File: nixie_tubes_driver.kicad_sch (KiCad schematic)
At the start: 17 parts, among them IC1 TPS61041DBVR, U1 CD40109BPW, U5 CD40109BPW, U6 HV5122PG-G, U7 HV5122PG-G

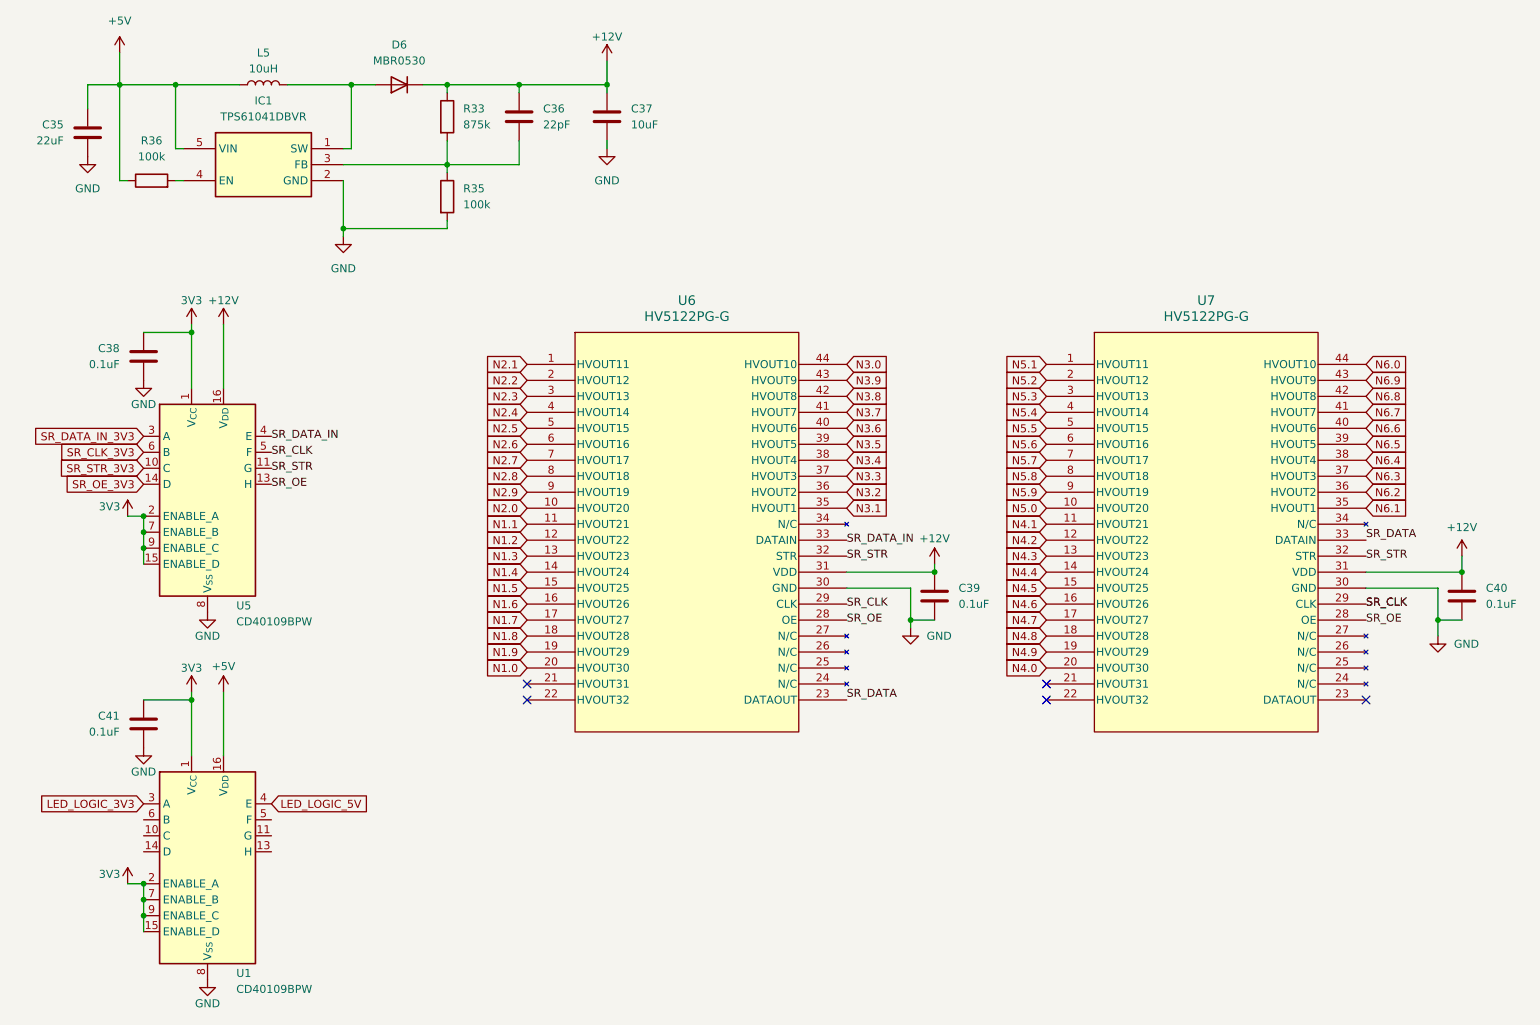
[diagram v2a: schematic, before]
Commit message: Begin positioning and grouping components
Add bypass caps to level shifters Vdd
Rearrange pins on shift register
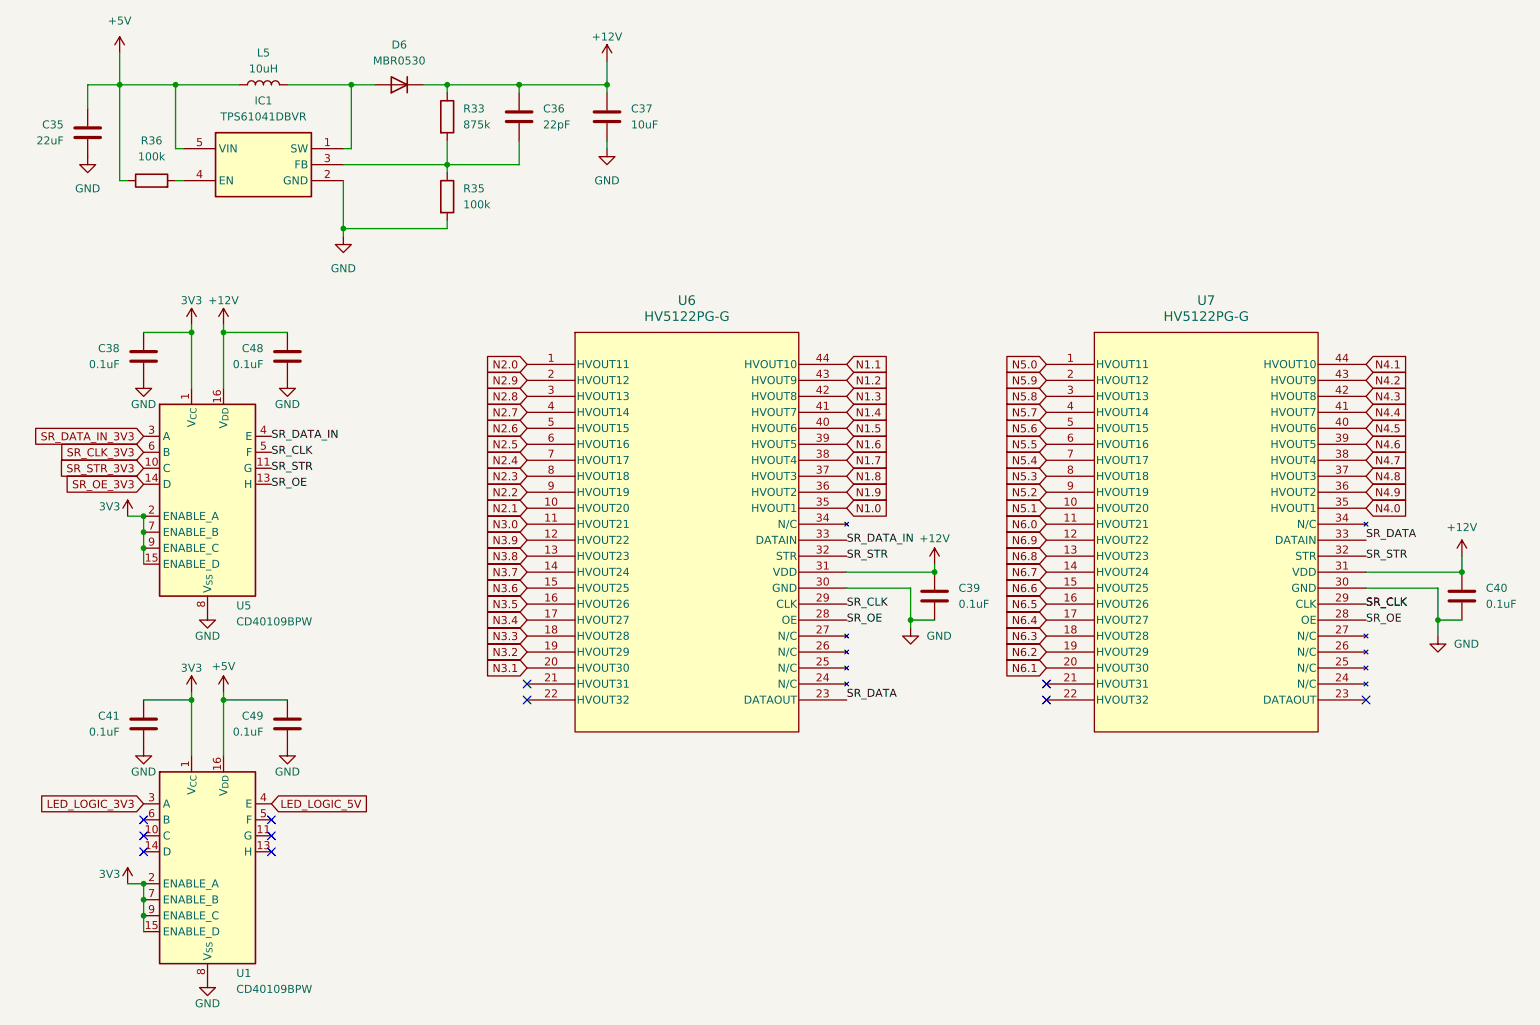
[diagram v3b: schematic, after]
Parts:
- added C48, C49: 0.1uF, Capacitor_SMD:C_0603_1608Metric, symbol Device:C
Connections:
- net +12V: now also C48.1
- net +5V: now also C49.1
- net GND: now also C48.2, C49.2
- net N1.0: now also U6.35 (HVOUT1); no longer U6.20 (HVOUT30)
- net N1.1: now also U6.44 (HVOUT10); no longer U6.11 (HVOUT21)
- net N1.2: now also U6.43 (HVOUT9); no longer U6.12 (HVOUT22)
- net N1.3: now also U6.42 (HVOUT8); no longer U6.13 (HVOUT23)
- net N1.4: now also U6.41 (HVOUT7); no longer U6.14 (HVOUT24)
- net N1.5: now also U6.40 (HVOUT6); no longer U6.15 (HVOUT25)
- net N1.6: now also U6.39 (HVOUT5); no longer U6.16 (HVOUT26)
- net N1.7: now also U6.38 (HVOUT4); no longer U6.17 (HVOUT27)
- net N1.8: now also U6.37 (HVOUT3); no longer U6.18 (HVOUT28)
- net N1.9: now also U6.36 (HVOUT2); no longer U6.19 (HVOUT29)
- net N2.0: now also U6.1 (HVOUT11); no longer U6.10 (HVOUT20)
- net N2.1: now also U6.10 (HVOUT20); no longer U6.1 (HVOUT11)
- net N2.2: now also U6.9 (HVOUT19); no longer U6.2 (HVOUT12)
- net N2.3: now also U6.8 (HVOUT18); no longer U6.3 (HVOUT13)
- net N2.4: now also U6.7 (HVOUT17); no longer U6.4 (HVOUT14)
- net N2.5: now also U6.6 (HVOUT16); no longer U6.5 (HVOUT15)
- net N2.6: now also U6.5 (HVOUT15); no longer U6.6 (HVOUT16)
- net N2.7: now also U6.4 (HVOUT14); no longer U6.7 (HVOUT17)
- net N2.8: now also U6.3 (HVOUT13); no longer U6.8 (HVOUT18)
- net N2.9: now also U6.2 (HVOUT12); no longer U6.9 (HVOUT19)
- net N3.0: now also U6.11 (HVOUT21); no longer U6.44 (HVOUT10)
- net N3.1: now also U6.20 (HVOUT30); no longer U6.35 (HVOUT1)
- net N3.2: now also U6.19 (HVOUT29); no longer U6.36 (HVOUT2)
- net N3.3: now also U6.18 (HVOUT28); no longer U6.37 (HVOUT3)
- net N3.4: now also U6.17 (HVOUT27); no longer U6.38 (HVOUT4)
- net N3.5: now also U6.16 (HVOUT26); no longer U6.39 (HVOUT5)
- net N3.6: now also U6.15 (HVOUT25); no longer U6.40 (HVOUT6)
- net N3.7: now also U6.14 (HVOUT24); no longer U6.41 (HVOUT7)
- net N3.8: now also U6.13 (HVOUT23); no longer U6.42 (HVOUT8)
- net N3.9: now also U6.12 (HVOUT22); no longer U6.43 (HVOUT9)
- net N4.0: now also U7.35 (HVOUT1); no longer U7.20 (HVOUT30)
- net N4.1: now also U7.44 (HVOUT10); no longer U7.11 (HVOUT21)
- net N4.2: now also U7.43 (HVOUT9); no longer U7.12 (HVOUT22)
- net N4.3: now also U7.42 (HVOUT8); no longer U7.13 (HVOUT23)
- net N4.4: now also U7.41 (HVOUT7); no longer U7.14 (HVOUT24)
- net N4.5: now also U7.40 (HVOUT6); no longer U7.15 (HVOUT25)
- net N4.6: now also U7.39 (HVOUT5); no longer U7.16 (HVOUT26)
- net N4.7: now also U7.38 (HVOUT4); no longer U7.17 (HVOUT27)
- net N4.8: now also U7.37 (HVOUT3); no longer U7.18 (HVOUT28)
- net N4.9: now also U7.36 (HVOUT2); no longer U7.19 (HVOUT29)
- net N5.0: now also U7.1 (HVOUT11); no longer U7.10 (HVOUT20)
- net N5.1: now also U7.10 (HVOUT20); no longer U7.1 (HVOUT11)
- net N5.2: now also U7.9 (HVOUT19); no longer U7.2 (HVOUT12)
- net N5.3: now also U7.8 (HVOUT18); no longer U7.3 (HVOUT13)
- net N5.4: now also U7.7 (HVOUT17); no longer U7.4 (HVOUT14)
- net N5.5: now also U7.6 (HVOUT16); no longer U7.5 (HVOUT15)
- net N5.6: now also U7.5 (HVOUT15); no longer U7.6 (HVOUT16)
- net N5.7: now also U7.4 (HVOUT14); no longer U7.7 (HVOUT17)
- net N5.8: now also U7.3 (HVOUT13); no longer U7.8 (HVOUT18)
- net N5.9: now also U7.2 (HVOUT12); no longer U7.9 (HVOUT19)
- net N6.0: now also U7.11 (HVOUT21); no longer U7.44 (HVOUT10)
- net N6.1: now also U7.20 (HVOUT30); no longer U7.35 (HVOUT1)
- net N6.2: now also U7.19 (HVOUT29); no longer U7.36 (HVOUT2)
- net N6.3: now also U7.18 (HVOUT28); no longer U7.37 (HVOUT3)
- net N6.4: now also U7.17 (HVOUT27); no longer U7.38 (HVOUT4)
- net N6.5: now also U7.16 (HVOUT26); no longer U7.39 (HVOUT5)
- net N6.6: now also U7.15 (HVOUT25); no longer U7.40 (HVOUT6)
- net N6.7: now also U7.14 (HVOUT24); no longer U7.41 (HVOUT7)
- net N6.8: now also U7.13 (HVOUT23); no longer U7.42 (HVOUT8)
- net N6.9: now also U7.12 (HVOUT22); no longer U7.43 (HVOUT9)
- no-connect marks 5 -> 11

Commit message: Add DigiKey part numbers to components
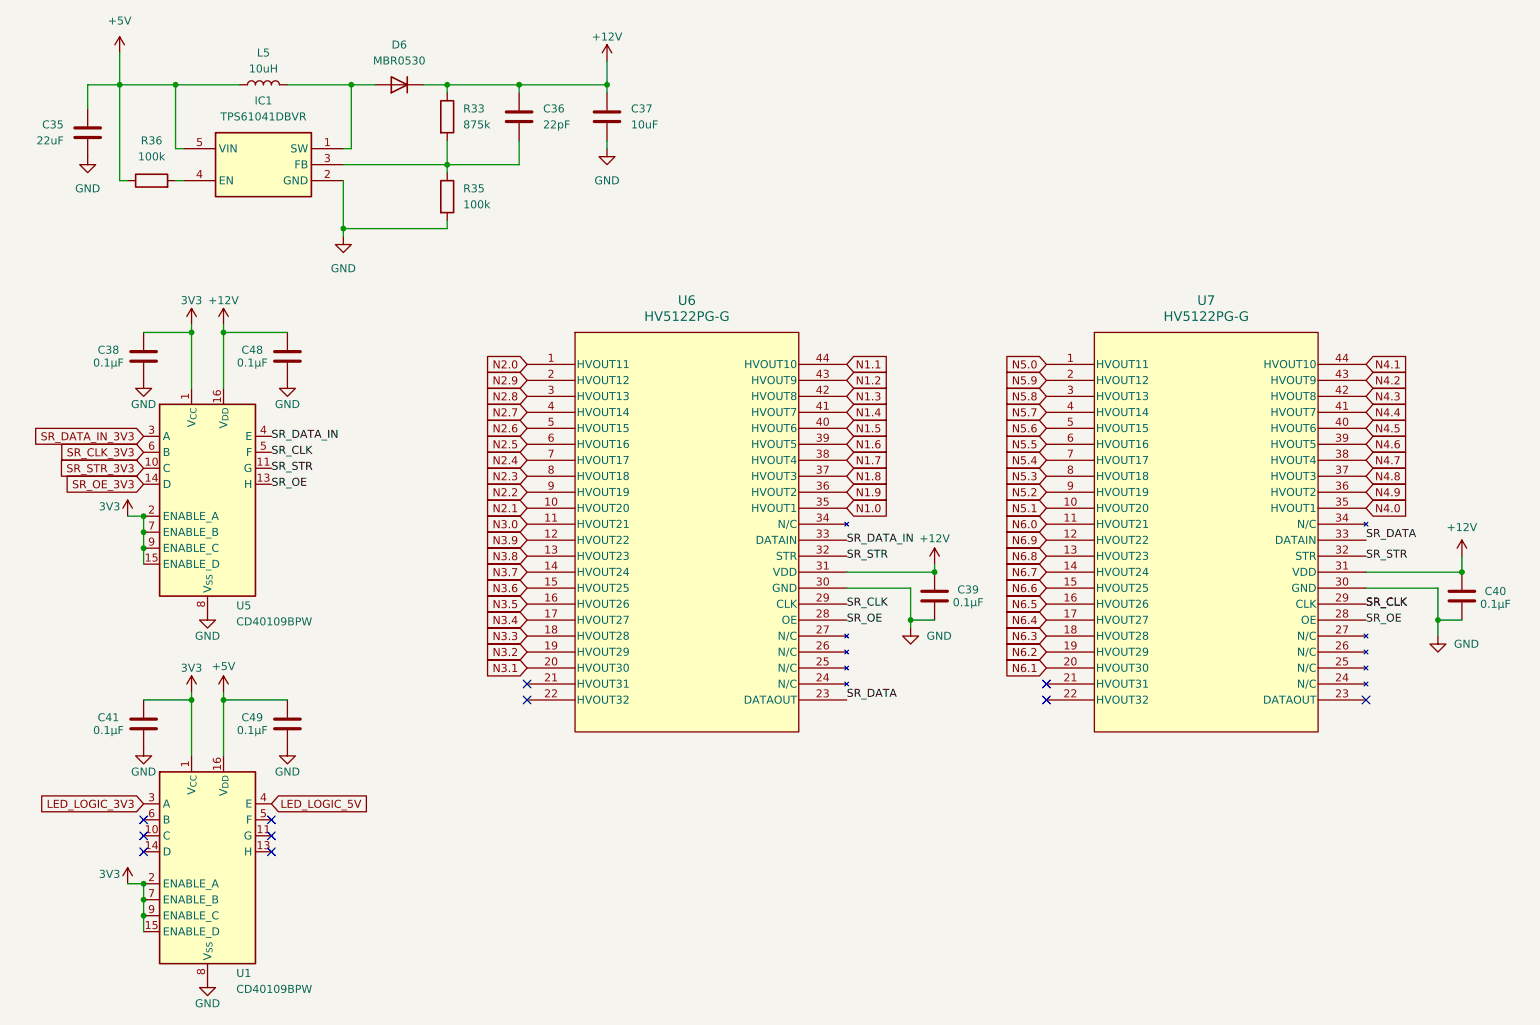
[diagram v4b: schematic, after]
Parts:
- C36: DigikeyPN (none) -> 399-C0603C220J5GACTUCT-ND
- C38, C39, C40, C41, C48, C49: value 0.1uF -> 0.1µF; DigikeyPN (none) -> 1276-1033-1-ND
- R33: footprint Resistor_SMD:R_0603_1608Metric -> Resistor_SMD:R_0805_2012Metric; DigikeyPN (none) -> 2019-RN73H2ATTD8763F10CT-ND
- R35, R36: DigikeyPN (none) -> 311-100KCRCT-ND
- U1, U5: DigikeyPN (none) -> 296-32859-5-ND
- U6, U7: DigikeyPN (none) -> HV5122PG-G-ND; DigkeyPN HV5122PG-G-ND -> (none)

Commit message: Fix 3V3/+3V3 nets; update pinouts for easier routing
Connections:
- net 3V3 renamed +3V3
